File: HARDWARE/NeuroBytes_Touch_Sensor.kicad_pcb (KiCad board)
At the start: 2 copper layers, 52.3 x 35.1 mm, 23 parts, among them P12 CONN_01X07, P6 CONN_01X04, P7 CONN_01X04, Q1 NPN_dual, Q2 NPN_dual, SW1 SW_PUSH, SW2 SW_PUSH, U1 STM32L011Gx, U2 LD3985G33R

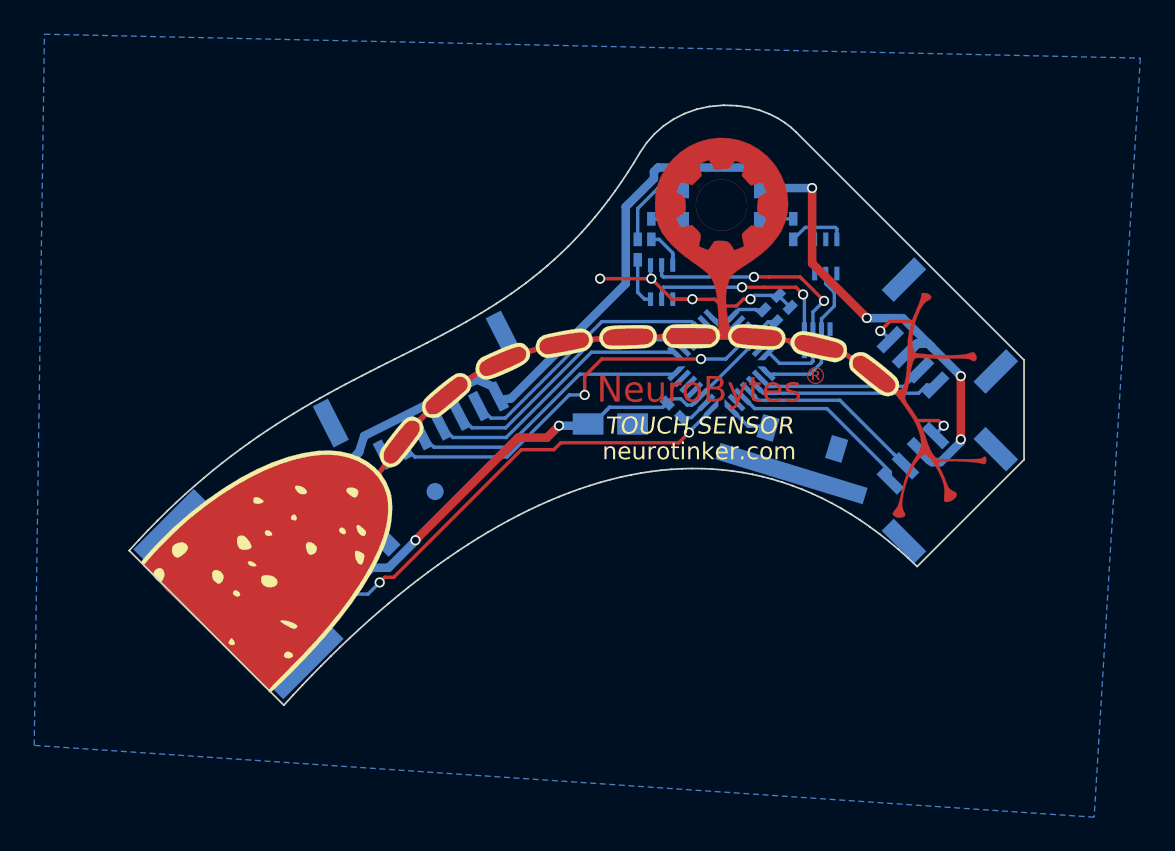
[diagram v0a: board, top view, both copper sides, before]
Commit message: Updated switch and connector footprints. Changed out dual transistors and resistor network for discrete components. Other minor updates.
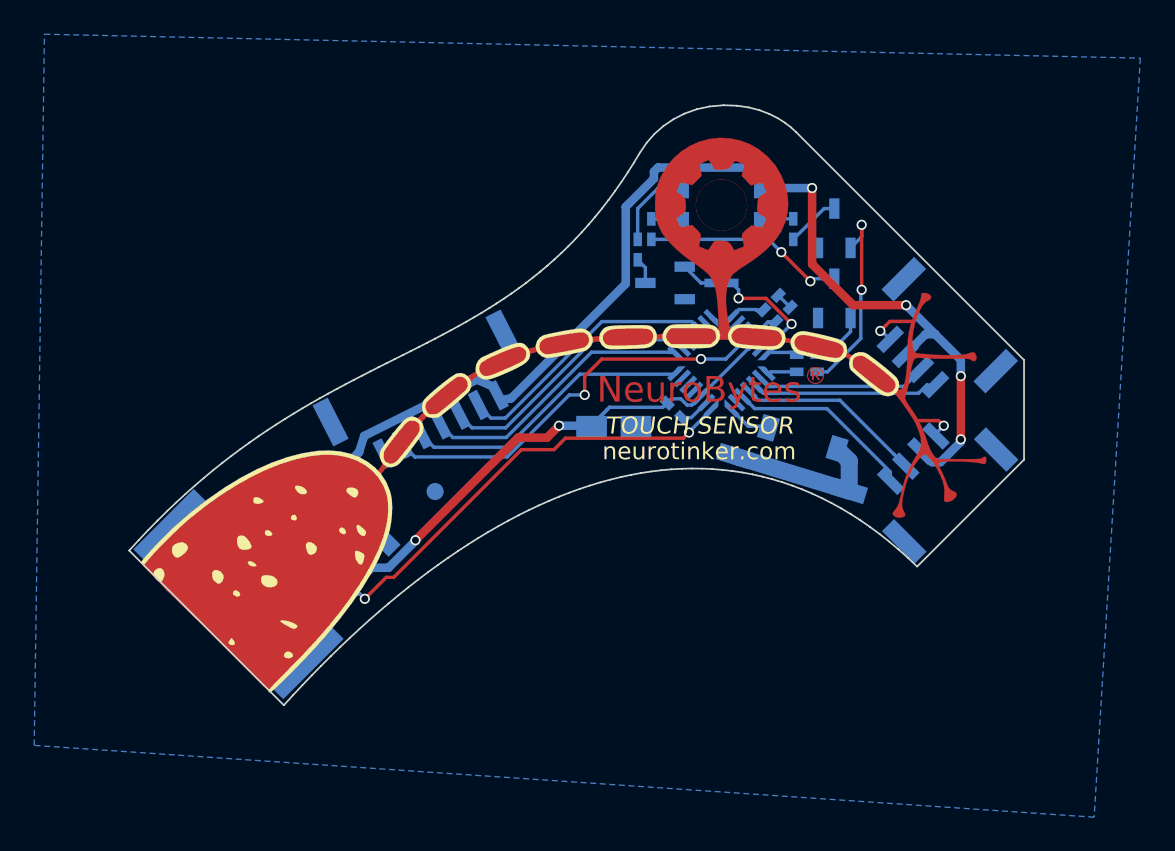
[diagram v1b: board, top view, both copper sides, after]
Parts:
- removed RN1: R_Pack04, KiCad_Footprints:ZF_RN_4iso_CTS-0804
- added Q3: MMBT3904, KiCad_Footprints:ZF_SOT23-3L, B.Cu at (133.1, 70.8)
- added R5: 1k, KiCad_Footprints:ZF_SMD_NonPol_0402, B.Cu at (126.5, 74.0)
- added R6: 1k, KiCad_Footprints:ZF_SMD_NonPol_0402, B.Cu at (131.5, 78.2)
- added R7: 1k, KiCad_Footprints:ZF_SMD_NonPol_0402, B.Cu at (131.5, 79.2)
- C1, C4: value C -> 1uF
- C2: value CP -> 10uF; footprint KiCad_Footprints:ZF_SMD_pol_1206 -> KiCad_Footprints:ZF_SMD_nonpol_1206
- C3: value C -> 100 nF
- C5: value C -> 0.1uF
- Q1, Q2: value NPN_dual -> MMBT3904; footprint KiCad_Footprints:ZF_SMD_SOT-363 -> KiCad_Footprints:ZF_SOT23-3L
- R1: value R -> 220
- R2, R3: value R -> 100
- R4: value R -> JMP
- SW2: value SW_PUSH -> SW_SNAP_ACTION
- moved Q2 2.50 mm to (133.1, 75.0), turned to 0 degrees
- moved SW1 1.71 mm to (131.0, 84.0)
- moved P12 0.74 mm to (109.3, 80.9)
- moved P6 0.69 mm to (138.9, 77.5)
- moved P7 0.67 mm to (138.9, 85.5)
- moved C2 0.25 mm to (120.2, 82.5)
- moved Q1 0.21 mm to (123.2, 74.0), turned to 90 degrees
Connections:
- Q1 pad 1: GND -> Net-(Q1-Pad1)
- Q1 pad 2: Net-(Q1-Pad2) -> GND
- Q2 pad 1: GND -> Net-(Q2-Pad1)
- Q2 pad 2: Net-(Q2-Pad2) -> GND
- R2 pad 2: Net-(Q1-Pad6) -> Net-(Q2-Pad3)
- R3 pad 2: Net-(Q2-Pad6) -> Net-(Q3-Pad3)
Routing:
- net Net-(Q1-Pad5): track 12.6 -> 0.00 mm, vias 2 -> 0
- net Net-(Q2-Pad3): track 0.00 -> 11.8 mm, vias 0 -> 2
- net Net-(Q3-Pad1): track 0.00 -> 11.6 mm, vias 0 -> 2
- net Net-(Q1-Pad2): track 11.1 -> 0.00 mm, vias 2 -> 0
- net LED_R: track 3.04 -> 7.18 mm, vias 0 -> 2
- net Net-(Q2-Pad2): track 3.77 -> 0.00 mm
- net GND: track 21.4 -> 17.9 mm, vias 6 -> 2
- net Net-(Q2-Pad6): track 3.48 -> 0.00 mm
- net Net-(Q2-Pad1): track 0.00 -> 3.31 mm
- net Net-(Q3-Pad3): track 0.00 -> 3.15 mm
- net Net-(Q1-Pad6): track 2.38 -> 0.00 mm
- net LED_B: track 4.03 -> 1.70 mm
- net Net-(Q1-Pad1): track 0.00 -> 1.94 mm
- net LED_G: track 3.49 -> 1.70 mm
- net Net-(Q1-Pad3): track 2.82 -> 1.54 mm
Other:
- net class Default: clearance 0.19 -> 0.2
- rule trace_clearance: 0.19 -> 0.2

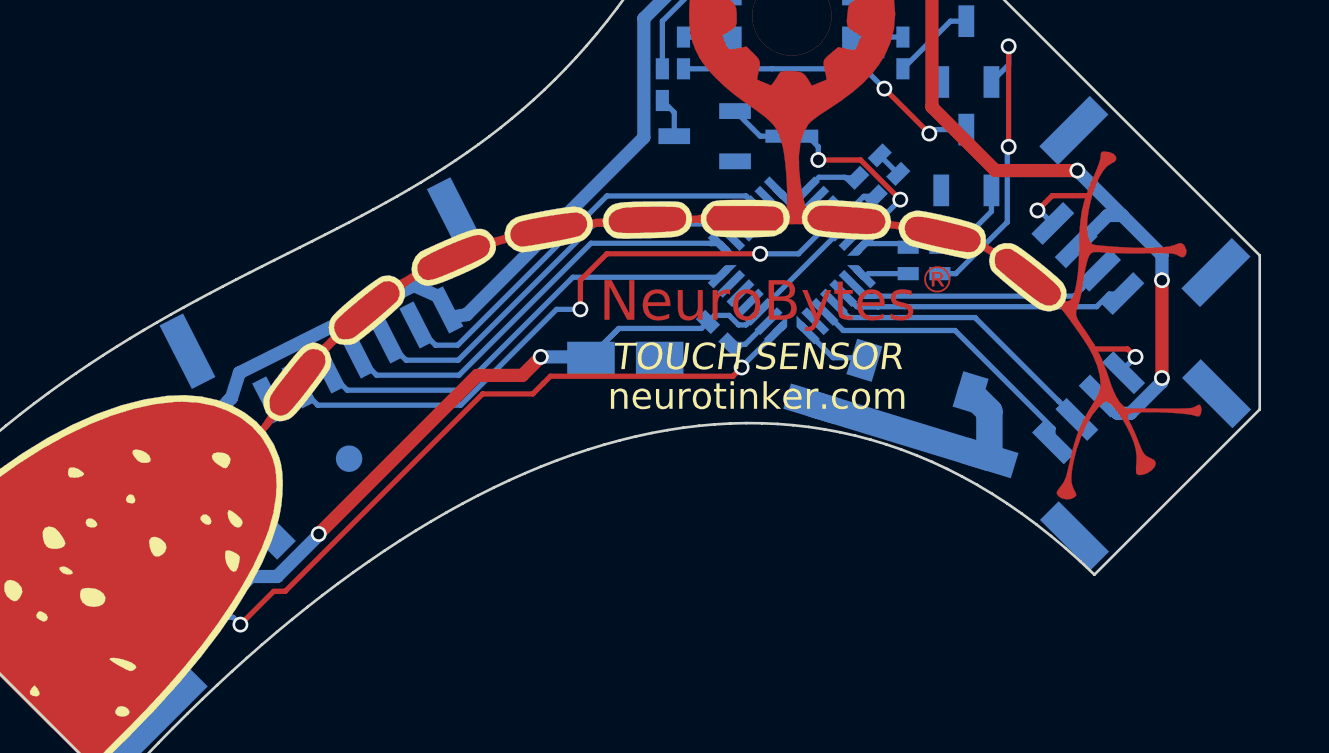
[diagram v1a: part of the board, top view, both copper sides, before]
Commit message: Switched to 5-pin power/programming connector. Added POWER text and increased ID text size. Changed to TOUCH SENSORY NEURON. Added dendrite ID letters.
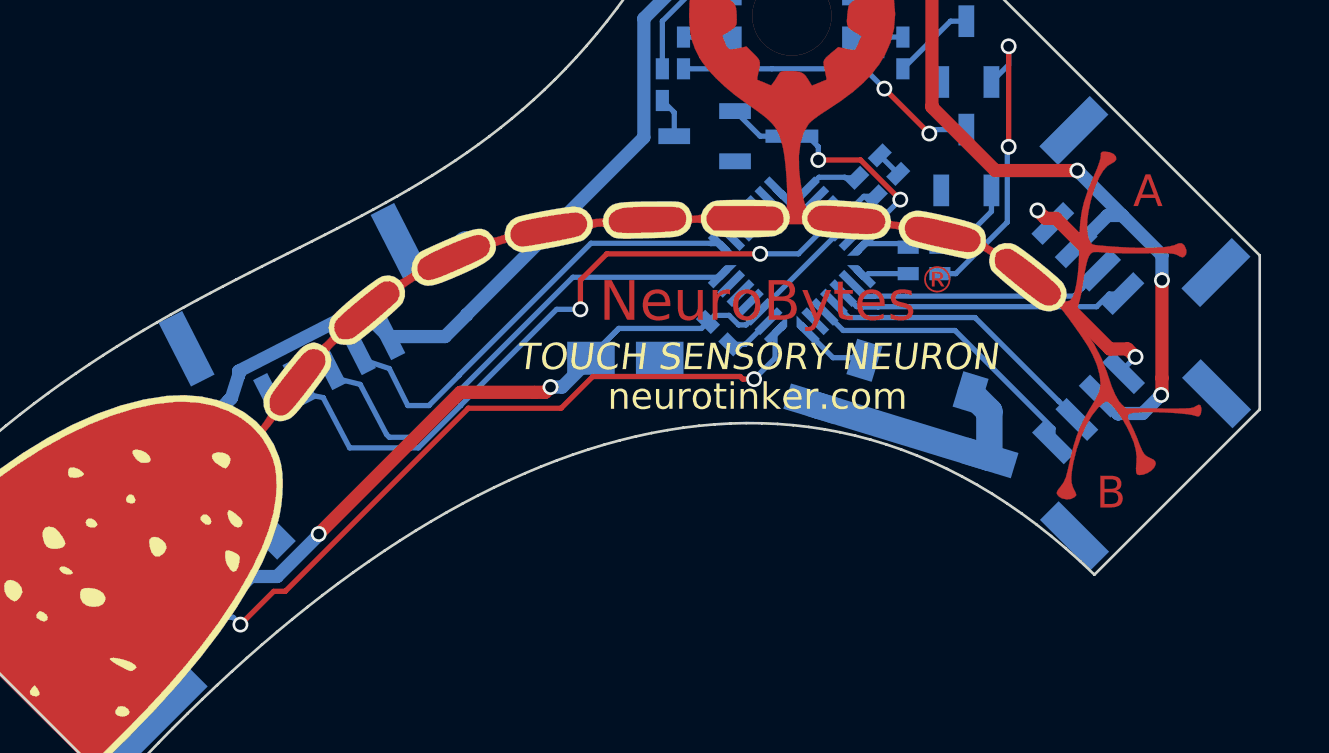
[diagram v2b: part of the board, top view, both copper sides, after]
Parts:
- removed P12: CONN_01X07, KiCad_Footprints:ZF_CONN_JST_GH_7POS
- added P1: JST_GH_5-pos, KiCad_Footprints:ZF_CONN_JST_GH_5POS, B.Cu at (108.3, 81.3)
- moved REF** 9.24 mm to (114.2, 78.1)
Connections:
- U1 pad 21: SWDIO/SCK -> SWDIO
- U1 pad 22: SWCLK/MISO -> SWCLK
- U1 pad 23: NSS -> Net-(U1-Pad23)
- U1 pad 26: MOSI -> Net-(U1-Pad26)
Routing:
- net SWDIO: track 0.00 -> 18.7 mm
- net SWCLK: track 0.00 -> 17.3 mm
- net SWDIO/SCK: track 16.8 -> 0.00 mm
- net SWCLK/MISO: track 16.0 -> 0.00 mm
- net MOSI: track 15.8 -> 0.00 mm
- net NSS: track 15.6 -> 0.00 mm
- net RESET: track 26.0 -> 27.8 mm
- net GND: track 17.9 -> 19.6 mm
- net INPUT: track 32.4 -> 33.0 mm
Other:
- board text added: "A"
- board text added: "B"
- board text added: "POWER"
- board text added: "TOUCH SENSORY NEURON"
- board text removed: "TOUCH SENSOR"

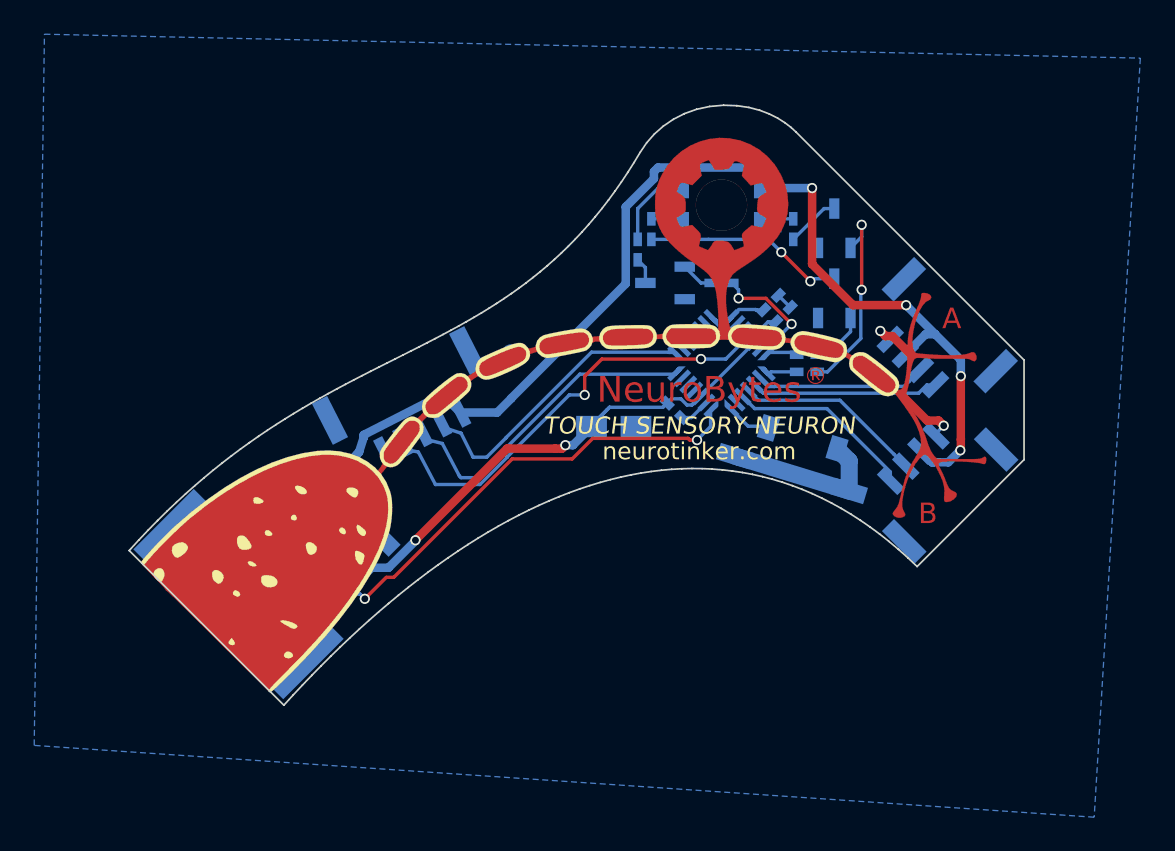
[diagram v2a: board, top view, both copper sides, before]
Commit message: updated gear shape to new design on PCB and *.svg. pulled mask back on labels. updated schematic part descriptions. fresh BOM export. other minor updates.
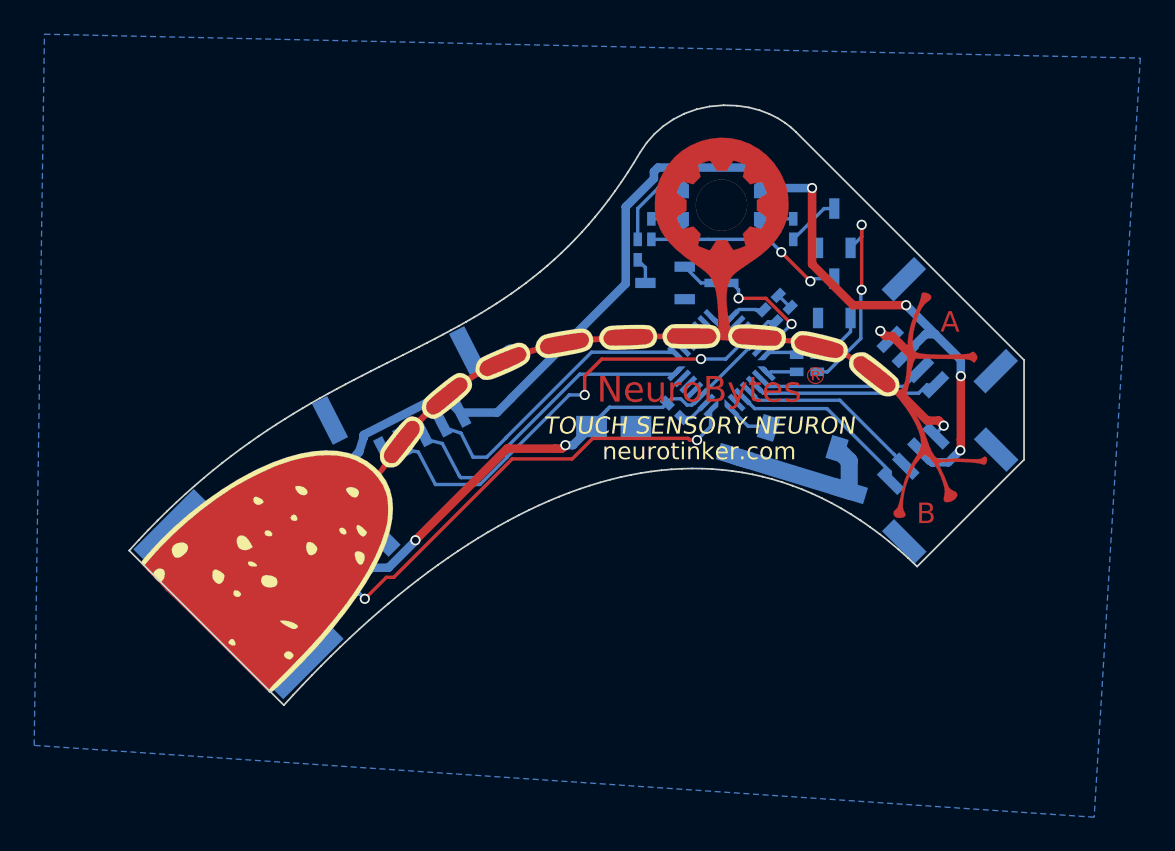
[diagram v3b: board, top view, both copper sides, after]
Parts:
- moved G*** 0.06 mm to (126.5, 69.5)

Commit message: reloaded netlist. minor PCB updates.
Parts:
- C1, C4: value 1uF -> 1u
- C2: value 10uF -> 10u
- C3: value 100 nF -> 0u1
- C5: value 0.1uF -> 0u1
- R1: value 220 -> 150
- U2: value LD3985G33R -> 3v3 LDO
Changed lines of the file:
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@@
 (kicad_pcb (version 4) (host pcbnew 4.0.7-e1-6374~58~ubuntu14.04.1)
   (general
-    (links 73)
+    (links 65)
     (no_connects 0)
-    (area 44.899999 43.8 172.928574 146.1)
+    (area 91.806226 63.606424 144.247748 98.799131)
     (thickness 1.6)
     (drawings 210)
@@
     (mod_text_size 1 1)
     (mod_text_width 0.15)
-    (pad_size 2 1)
+    (pad_size 1 2.7)
     (pad_drill 0)
     (pad_to_mask_clearance 0)
@@
   (module KiCad_Footprints:ZF_LOGO_Touch_Sensor (layer F.Cu)
     (at 126.49 69.46)
+    (attr smd)
     (fp_text reference G*** (at 0 0) (layer F.SilkS) hide
       (effects (font (thickness 0.3)))
@@
       (effects (font (size 1 1) (thickness 0.15)) (justify mirror))
     )
-    (fp_text value 1uF (at 0 4.7 225) (layer B.Fab) hide
+    (fp_text value 1u (at 0 4.7 225) (layer B.Fab) hide
       (effects (font (size 1 1) (thickness 0.15)) (justify mirror))
     )
@@
       (effects (font (size 1 1) (thickness 0.15)) (justify mirror))
     )
-    (fp_text value "100 nF" (at 0 1.5 315) (layer B.Fab) hide
+    (fp_text value 0u1 (at 0 1.5 315) (layer B.Fab) hide
       (effects (font (size 1 1) (thickness 0.15)) (justify mirror))
     )
@@
       (effects (font (size 1 1) (thickness 0.15)) (justify mirror))
     )
-    (fp_text value 1uF (at 0 4.7 45) (layer B.Fab) hide
+    (fp_text value 1u (at 0 4.7 45) (layer B.Fab) hide
       (effects (font (size 1 1) (thickness 0.15)) (justify mirror))
     )
@@
       (effects (font (size 1 1) (thickness 0.15)) (justify mirror))
     )
-    (fp_text value 0.1uF (at 0 1.5 45) (layer B.Fab) hide
+    (fp_text value 0u1 (at 0 1.5 45) (layer B.Fab) hide
       (effects (font (size 1 1) (thickness 0.15)) (justify mirror))
     )
@@
       (effects (font (size 1 1) (thickness 0.15)) (justify mirror))
     )
-    (fp_text value 220 (at 0 1.5 270) (layer B.Fab) hide
+    (fp_text value 150 (at 0 1.5 270) (layer B.Fab) hide
       (effects (font (size 1 1) (thickness 0.15)) (justify mirror))
     )
@@
       (effects (font (size 1 1) (thickness 0.15)) (justify mirror))
     )
-    (fp_text value LD3985G33R (at 0 3.5 315) (layer B.Fab) hide
+    (fp_text value "3v3 LDO" (at 0 3.5 315) (layer B.Fab) hide
       (effects (font (size 1 1) (thickness 0.15)) (justify mirror))
     )
@@
       (effects (font (size 1 1) (thickness 0.15)) (justify mirror))
     )
-    (fp_text value 10uF (at 0 3.6) (layer B.Fab) hide
-      (effects (font (size 1 1) (thickness 0.15)) (justify mirror))
-    )
+    (fp_text value 10u (at 0 3.6) (layer B.Fab) hide
+      (effects (font (size 1 1) (thickness 0.15)) (justify mirror))
+    )

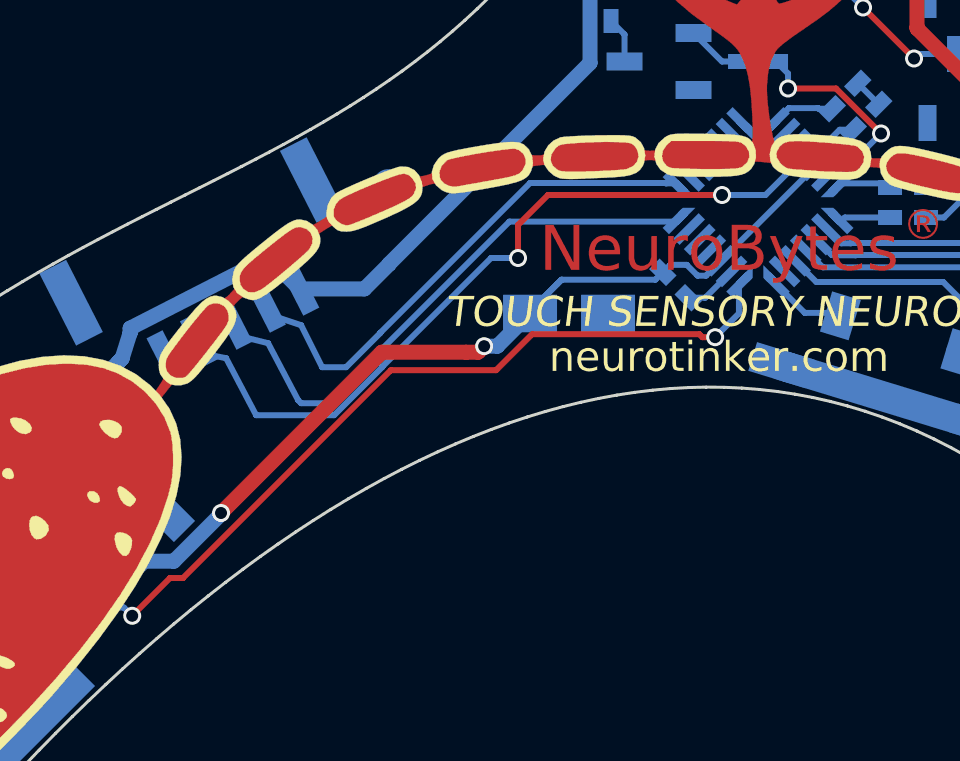
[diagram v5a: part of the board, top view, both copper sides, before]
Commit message: added ESD protection. minor routing changes. updated title block.
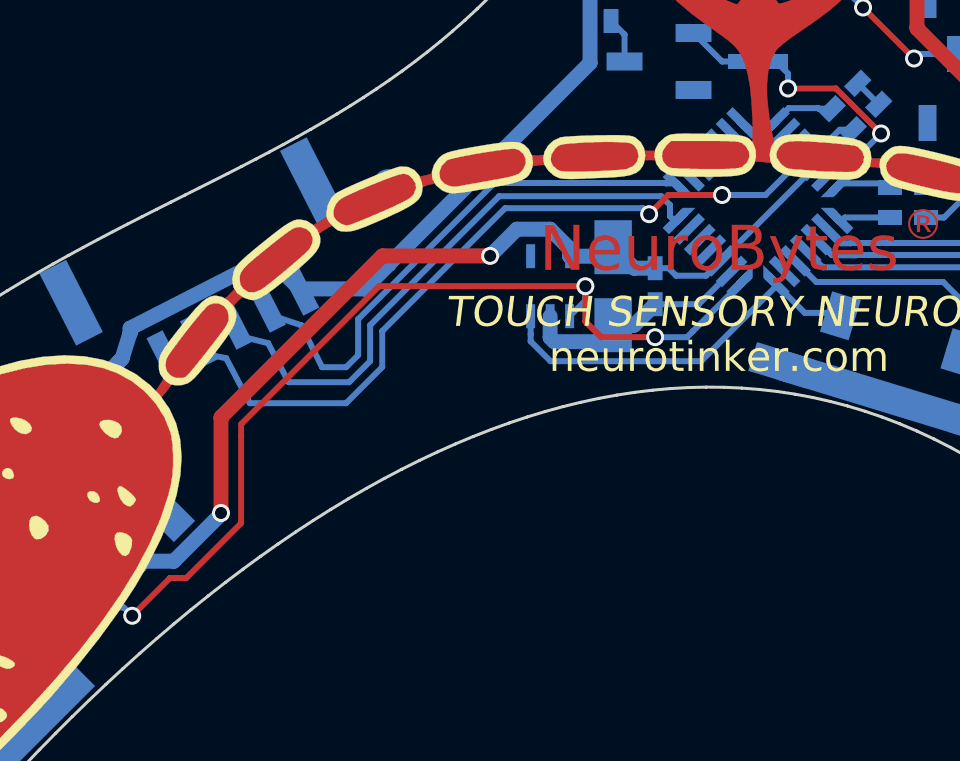
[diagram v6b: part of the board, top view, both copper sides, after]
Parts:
- added U3: RClamp0503F, KiCad_Footprints:ZF_SMD_SOT-353, B.Cu at (119.6, 81.5)
- moved C2 1.73 mm to (121.7, 81.5), turned to 270 degrees
- moved C3 0.68 mm to (123.1, 81.5), turned to 270 degrees
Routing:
- net IDENTIFY: track 2.37 -> 12.7 mm
- net GND: track 19.6 -> 25.6 mm
- net INPUT: track 33.0 -> 38.1 mm, vias 2 -> 3
- net +3V3: track 34.9 -> 36.6 mm
- net SWDIO: track 18.7 -> 19.6 mm
- net SWCLK: track 17.3 -> 18.0 mm
